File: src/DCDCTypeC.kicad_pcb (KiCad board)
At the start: 2 copper layers, 24 x 36 mm, 22 parts, among them J1 ‎USB4085, J2 MCV 1,5/2

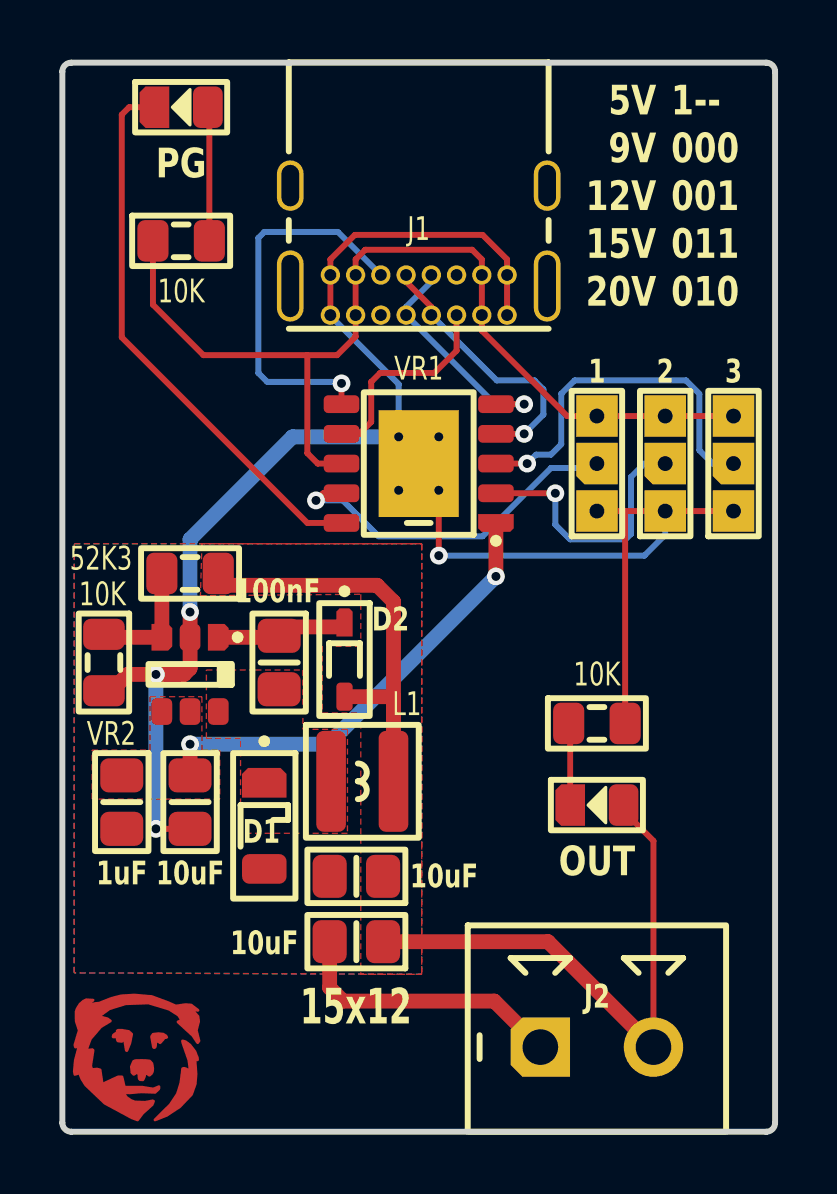
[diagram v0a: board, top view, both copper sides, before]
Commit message: Added test points
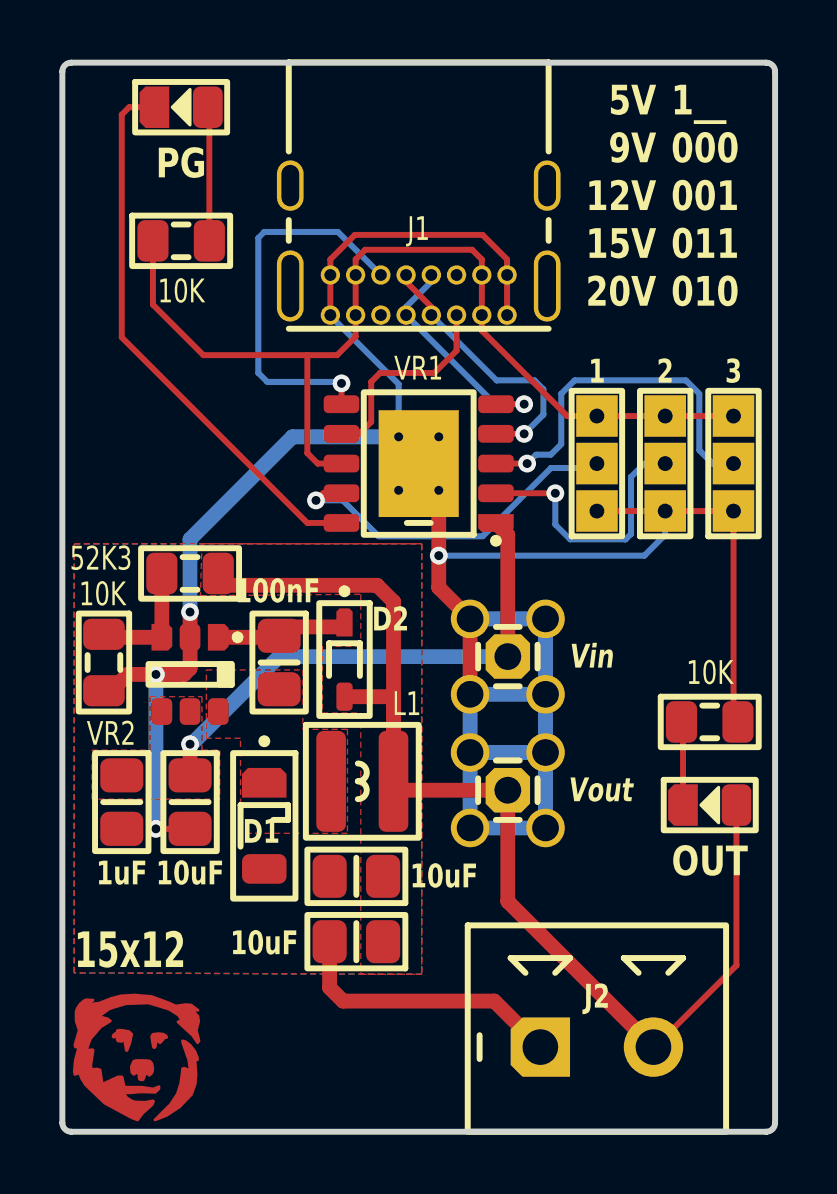
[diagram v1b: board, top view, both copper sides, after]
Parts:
- added TP1: Vin, Medo64:TP MMCX (3.5mm), F.Cu at (35.0, 40.0)
- added TP2: Vout, Medo64:TP MMCX (3.5mm), F.Cu at (35.0, 44.5)
- moved R2 3.80 mm to (41.8, 42.2)
- moved DS2 3.80 mm to (41.8, 45.0)
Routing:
- net GND: track 76.2 -> 104.8 mm
- net Vout: track 36.2 -> 40.6 mm
- net Vin: track 15.5 -> 17.6 mm, vias 2 -> 1
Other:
- board text added: "1__ 000 001 011 010"
- board text removed: "1-- 000 001 011 010"
